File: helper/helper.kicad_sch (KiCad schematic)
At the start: 41 parts, among them J1 Conn_02x34_Odd_Even, J2 Conn_01x08_Male

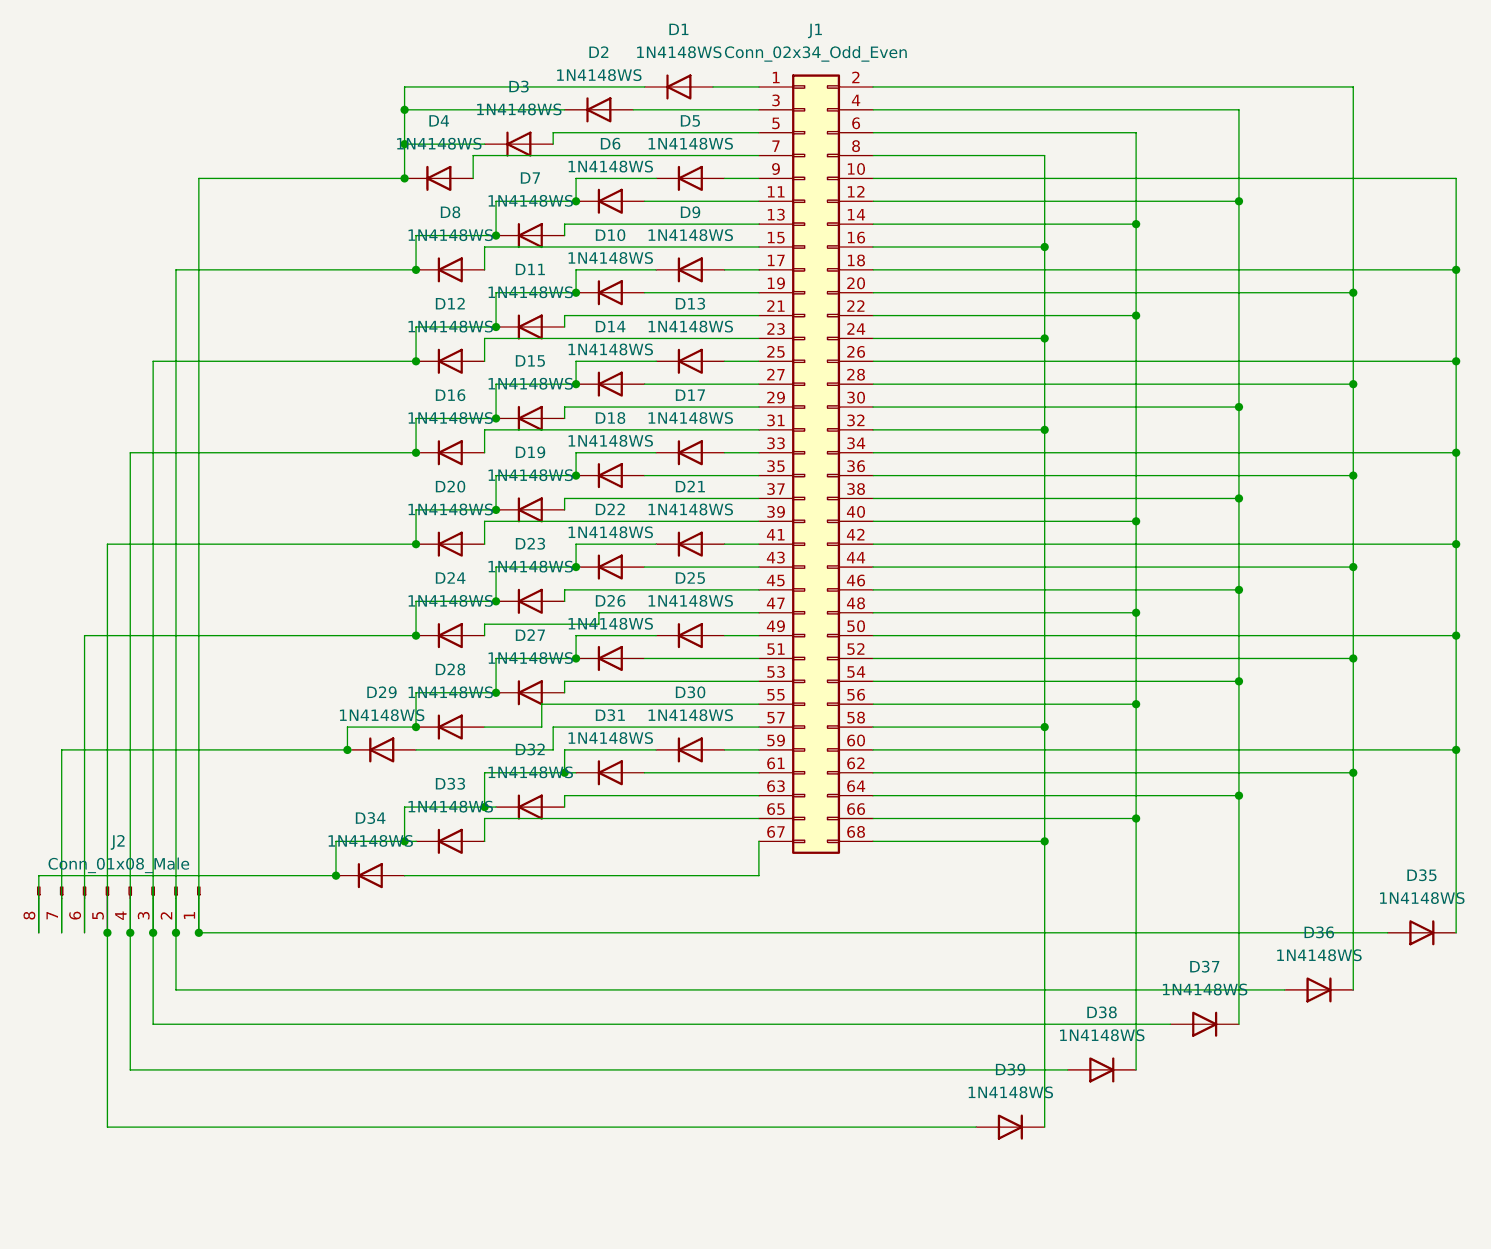
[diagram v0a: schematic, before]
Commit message: handwire helper for 4/5 x 8 standard matrix with through-hole diodes and ground fill
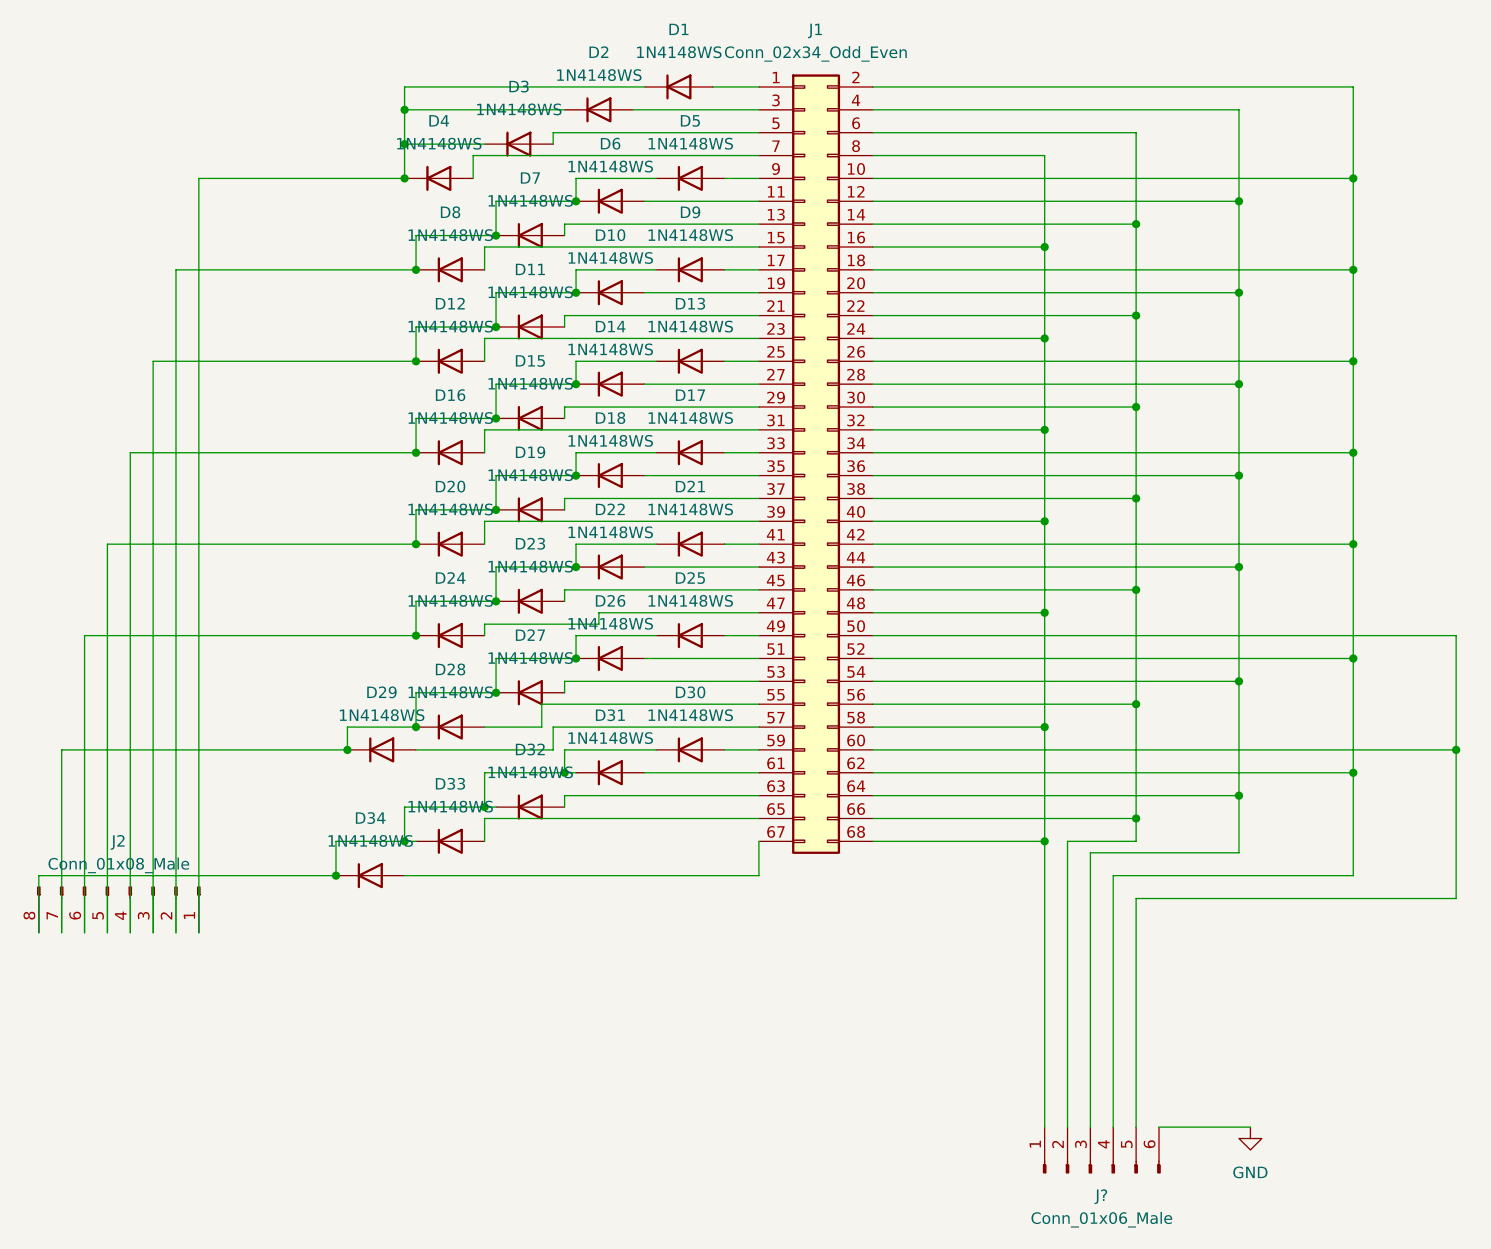
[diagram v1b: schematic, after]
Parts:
- removed D35, D36, D37, D38, D39: 1N4148WS, Diode_SMD:D_SOD-323, symbol Diode:1N4148WS
- added J?: Conn_01x06_Male, symbol Connector:Conn_01x06_Male
- D1, D10, D11, D12, D13, D14, D15, D16, D17, D18, D19, D2, D20, D21, D22, D23, D24, D25, D26, D27, D28, D29, D3, D30, D31, D32, D33, D34, D4, D5, D6, D7, D8, D9: footprint Diode_SMD:D_SOD-323 -> Diode_THT:D_DO-35_SOD27_P7.62mm_Horizontal
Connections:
- net at J1.12 (Pin_12), J1.4 (Pin_4), J1.54 (Pin_54)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: now also J1.20 (Pin_20), J1.28 (Pin_28), J1.36 (Pin_36), J1.44 (Pin_44), J?.3 (Pin_3); no longer J1.30 (Pin_30), J1.38 (Pin_38), J1.46 (Pin_46)
- net at J1.10 (Pin_10), J1.18 (Pin_18), J1.26 (Pin_26)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: now also J1.2 (Pin_2), J1.52 (Pin_52), J1.62 (Pin_62), J?.4 (Pin_4); no longer J1.50 (Pin_50), J1.60 (Pin_60)
- net at J1.14 (Pin_14), J1.22 (Pin_22), J1.56 (Pin_56)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: now also J1.30 (Pin_30), J1.38 (Pin_38), J1.46 (Pin_46), J?.2 (Pin_2); no longer J1.40 (Pin_40), J1.48 (Pin_48)
- net at J1.16 (Pin_16), J1.24 (Pin_24), J1.32 (Pin_32)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: now also J1.40 (Pin_40), J1.48 (Pin_48), J?.1 (Pin_1)
- new net: J1.50 (Pin_50), J1.60 (Pin_60), J?.5 (Pin_5)
- new net GND: J?.6 (Pin_6)

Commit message: Handwire Helper version 0.1 as submitted
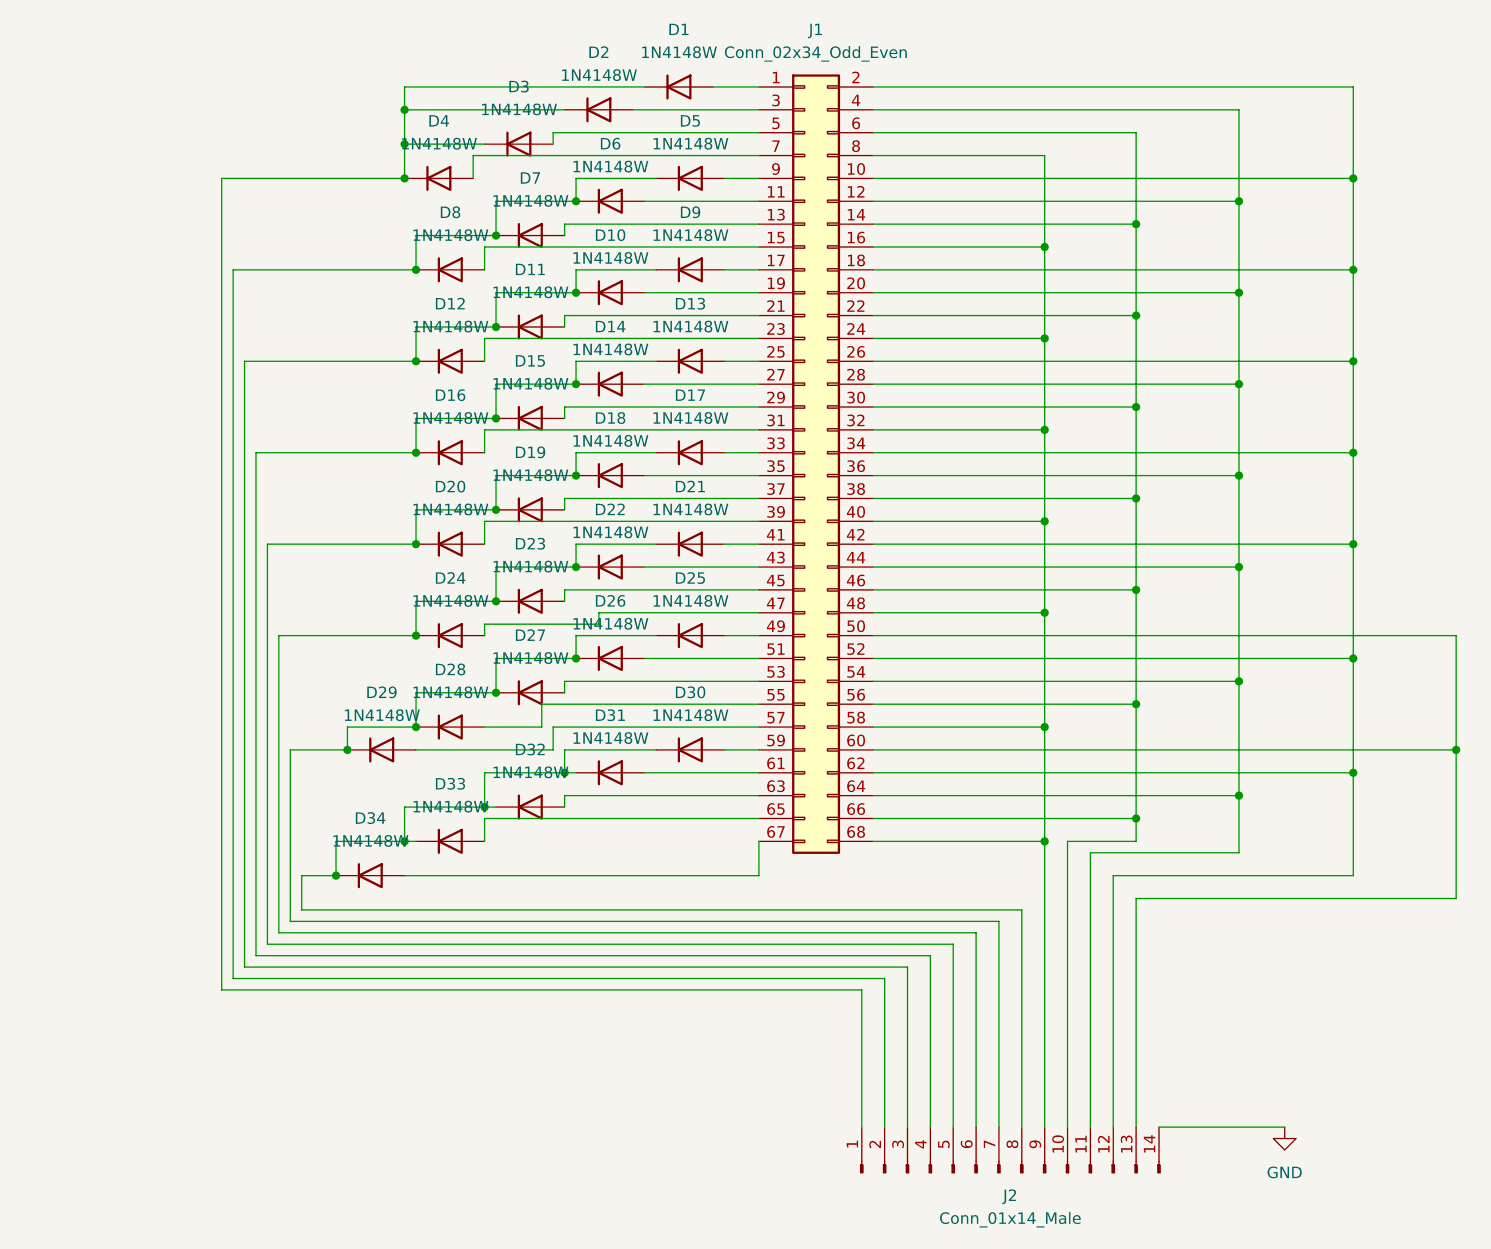
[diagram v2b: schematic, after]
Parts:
- removed J2: Conn_01x08_Male, Connector_PinHeader_2.54mm:PinHeader_2x04_P2.54mm_Horizontal, symbol Connector:Conn_01x08_Male
- removed J?: Conn_01x06_Male, symbol Connector:Conn_01x06_Male
- added J2: Conn_01x14_Male, Connector_PinHeader_2.54mm:PinHeader_2x07_P2.54mm_Horizontal, symbol Connector:Conn_01x14_Male
- D1, D10, D11, D12, D13, D14, D15, D16, D17, D18, D19, D2, D20, D21, D22, D23, D24, D25, D26, D27, D28, D29, D3, D30, D31, D32, D33, D34, D4, D5, D6, D7, D8, D9: value 1N4148WS -> 1N4148W; footprint Diode_THT:D_DO-35_SOD27_P7.62mm_Horizontal -> handy:Reversable_Diode_SOD-123_THT
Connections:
- net GND: now also J2.14 (Pin_14)
- net at D30.1 (K), D31.1 (K), D32.1 (K)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: now also J2.8 (Pin_8)
- net at D10.1 (K), D11.1 (K), D12.1 (K)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: now also J2.3 (Pin_3)
- net at D5.1 (K), D6.1 (K), D7.1 (K)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: now also J2.2 (Pin_2)
- net at D17.1 (K), D18.1 (K), D19.1 (K)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: now also J2.5 (Pin_5)
- net at D25.1 (K), D26.1 (K), D27.1 (K)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: now also J2.7 (Pin_7)
- net at D1.1 (K), D2.1 (K), D3.1 (K)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: now also J2.1 (Pin_1)
- net at D13.1 (K), D14.1 (K), D15.1 (K)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: now also J2.4 (Pin_4)
- net at D21.1 (K), D22.1 (K), D23.1 (K)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: now also J2.6 (Pin_6)
- net at J1.10 (Pin_10), J1.18 (Pin_18), J1.2 (Pin_2)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: now also J2.12 (Pin_12)
- net at J1.12 (Pin_12), J1.20 (Pin_20), J1.28 (Pin_28)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: now also J2.11 (Pin_11)
- net at J1.14 (Pin_14), J1.22 (Pin_22), J1.30 (Pin_30)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: now also J2.10 (Pin_10)
- net at J1.16 (Pin_16), J1.24 (Pin_24), J1.32 (Pin_32)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: now also J2.9 (Pin_9)
- net at J1.50 (Pin_50), J1.60 (Pin_60): now also J2.13 (Pin_13)
